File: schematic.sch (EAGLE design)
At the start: 32 parts, among them U1 ADP3338AKCZ-3.3RL7

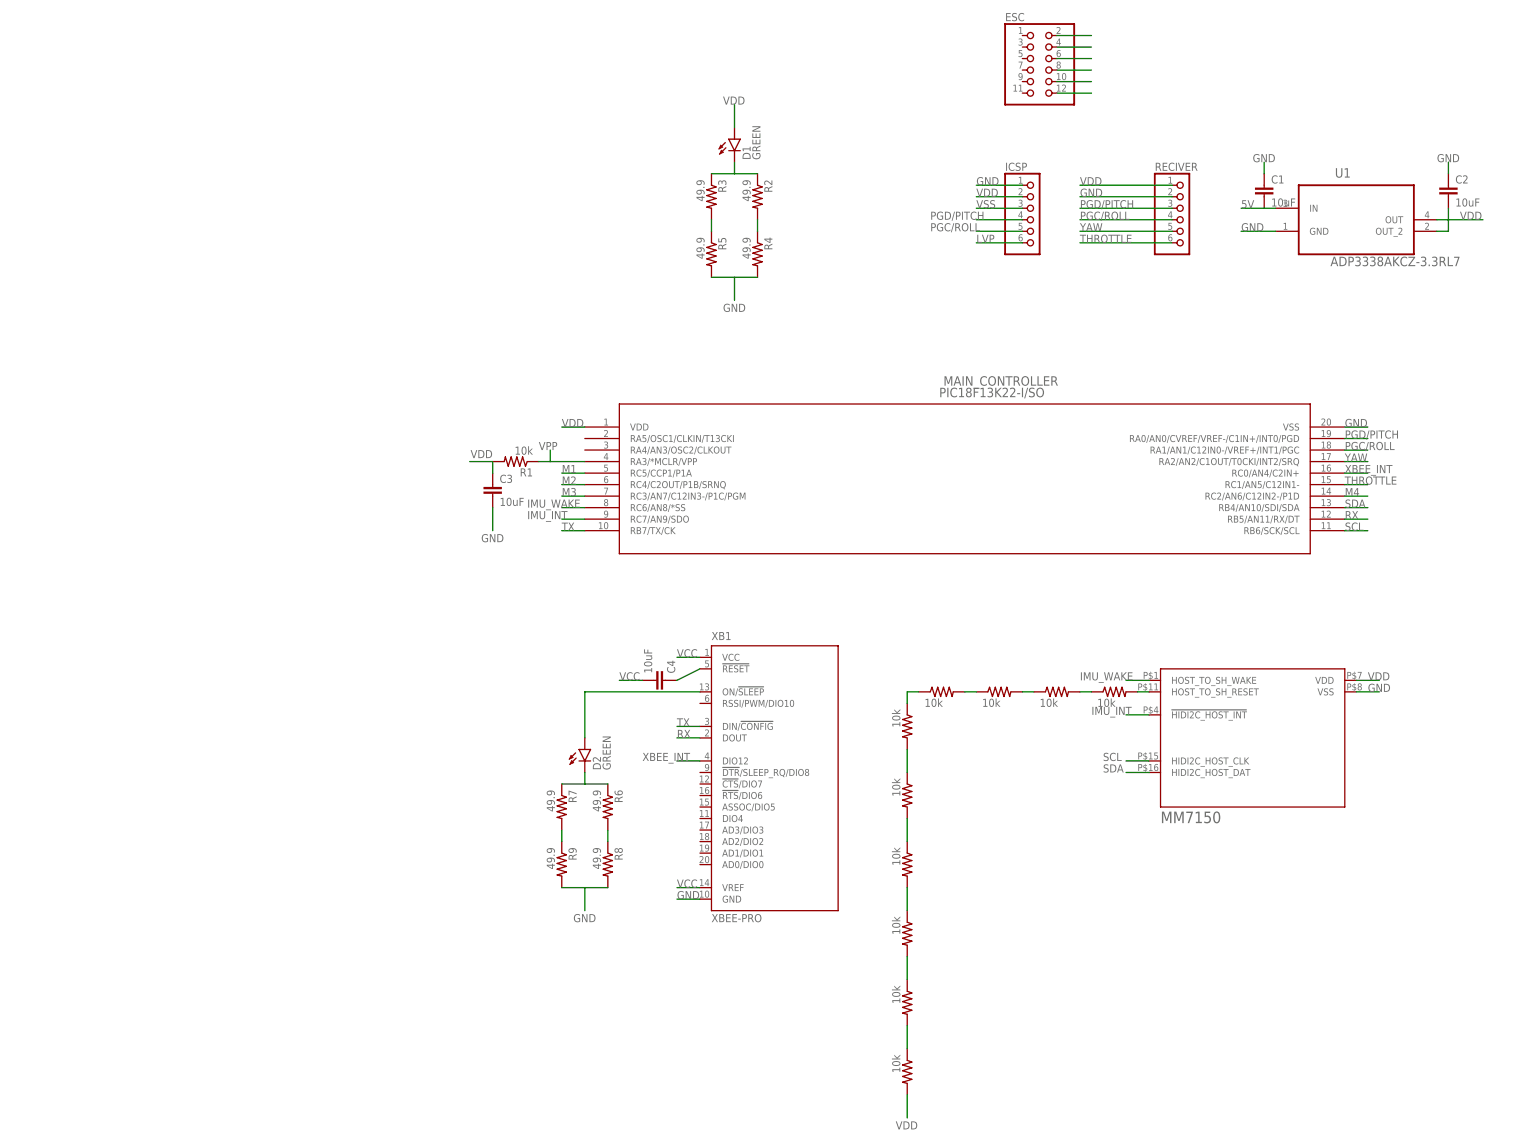
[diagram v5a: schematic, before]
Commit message: Added several missing components, rearanged some components to make routing easier and added last jumper cables. Board layout is theretically done now
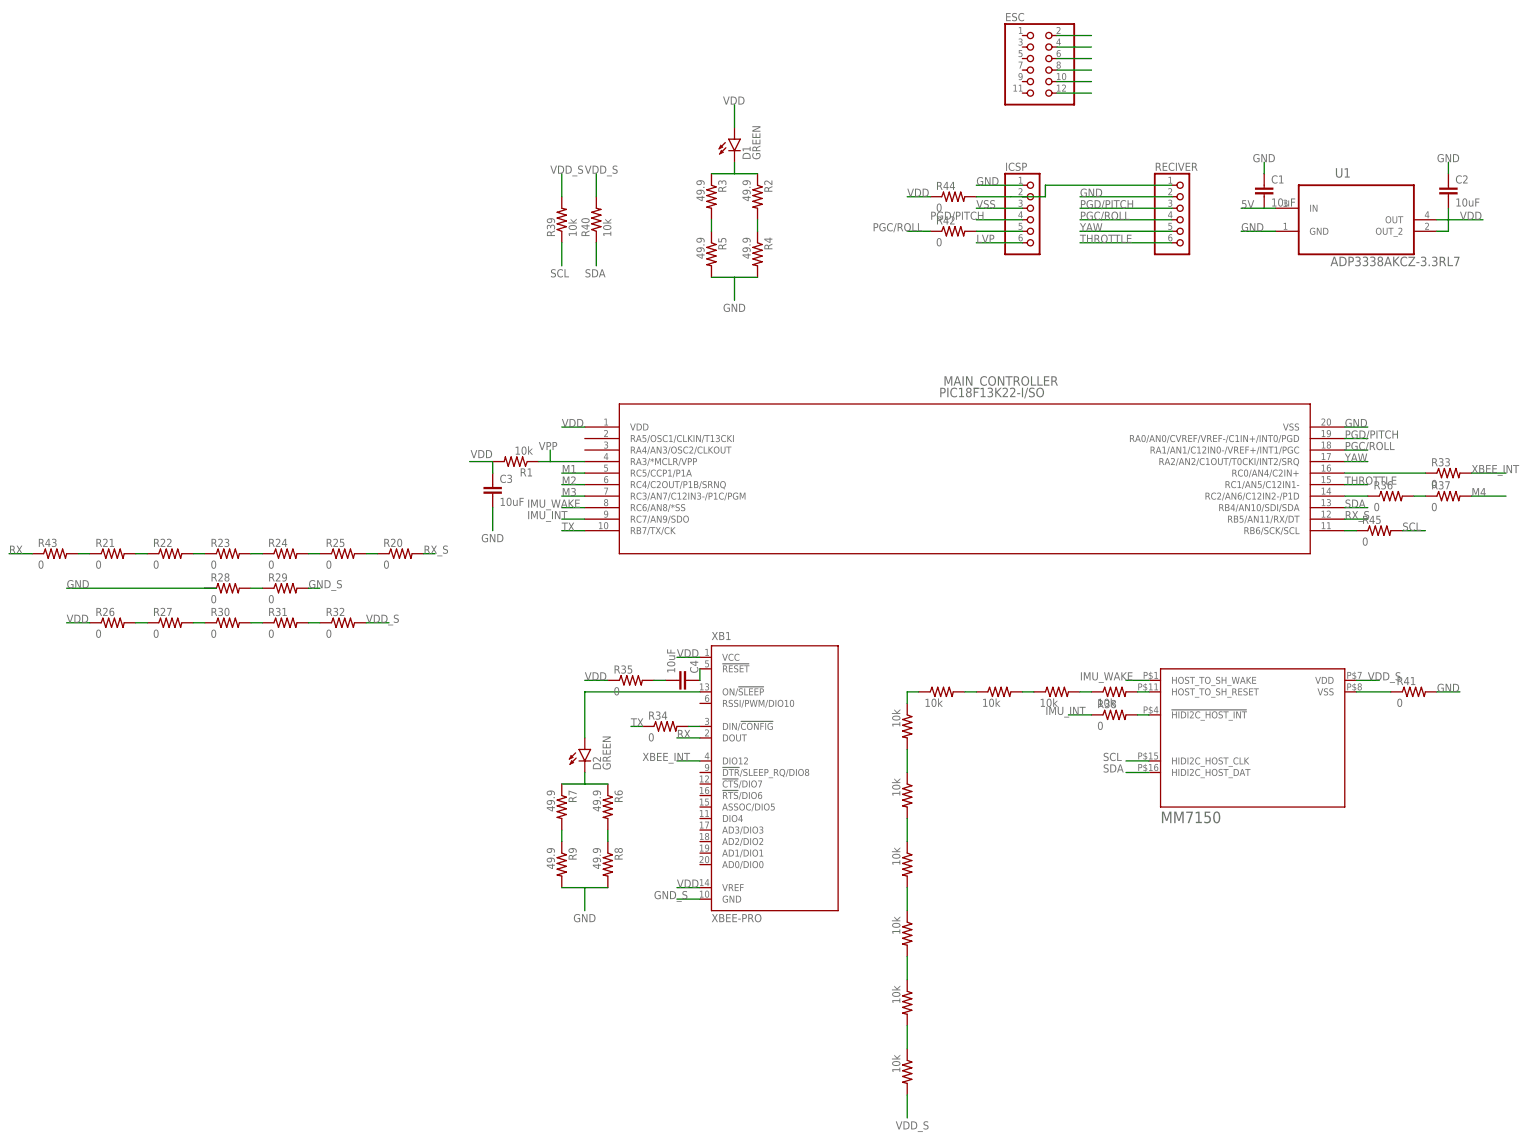
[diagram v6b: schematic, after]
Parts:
- added R20, R21, R22, R23, R24, R25, R26, R27, R28, R29, R30, R31, R32, R33, R34, R35, R36, R37, R38, R41, R42, R43, R44, R45: 0, SparkFun-Passives:RESISTOR0603-RES
- added R39, R40: 10k, SparkFun-Passives:RESISTOR0402-RES
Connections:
- removed net VCC: C4.2, XB1.VCC, XB1.VREF
- new net GND_S: R29.2, XB1.GND
- new net N$1: R20.1, R25.2
- new net N$20: R21.2, R22.1
- new net N$21: R22.2, R23.1
- new net N$22: R23.2, R24.1
- new net N$23: R24.2, R25.1
- new net N$24: R28.2, R29.1
- new net N$25: MAIN_CONTROLLER.RC0/AN4/C2IN+, R33.1
- new net N$26: R26.2, R27.1
- new net N$27: R27.2, R30.1
- new net N$28: R30.2, R31.1
- new net N$29: R31.2, R32.1
- new net N$30: R34.2, XB1.DIN/!CONFIG
- new net N$31: C4.2, R35.2
- new net N$32: MAIN_CONTROLLER.RC2/AN6/C12IN2-/P1D, R36.1
- new net N$33: R36.2, R37.1
- new net N$34: IMU.!HIDI2C_HOST_INT, R38.2
- new net N$35: IMU.VSS, R41.1
- new net N$36: R21.1, R43.2
- new net N$37: ICSP.5, R42.2
- new net N$38: ICSP.2, R44.2, RECIVER.1
- new net N$39: MAIN_CONTROLLER.RB6/SCK/SCL, R45.1
- new net RX_S: MAIN_CONTROLLER.RB5/AN11/RX/DT, R20.2
- new net VDD_S: IMU.VDD, R19.2, R32.2, R39.2, R40.2
- net GND: now also R28.1, R41.2; no longer IMU.VSS, XB1.GND
- net IMU_INT: now also R38.1; no longer IMU.!HIDI2C_HOST_INT
- net M4: now also R37.2; no longer MAIN_CONTROLLER.RC2/AN6/C12IN2-/P1D
- net PGC/ROLL: now also R42.1; no longer ICSP.5
- net RX: now also R43.1; no longer MAIN_CONTROLLER.RB5/AN11/RX/DT
- net SCL: now also R39.1, R45.2; no longer MAIN_CONTROLLER.RB6/SCK/SCL
- net SDA: now also R40.1
- net TX: now also R34.1; no longer XB1.DIN/!CONFIG
- net VDD: now also R26.1, R35.1, R44.1, XB1.VCC, XB1.VREF; no longer ICSP.2, IMU.VDD, R19.2, RECIVER.1
- net XBEE_INT: now also R33.2; no longer MAIN_CONTROLLER.RC0/AN4/C2IN+
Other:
- moved on the sheet: C4
